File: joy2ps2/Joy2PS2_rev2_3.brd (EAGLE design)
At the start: 78.7 x 67.3 mm, 7 parts

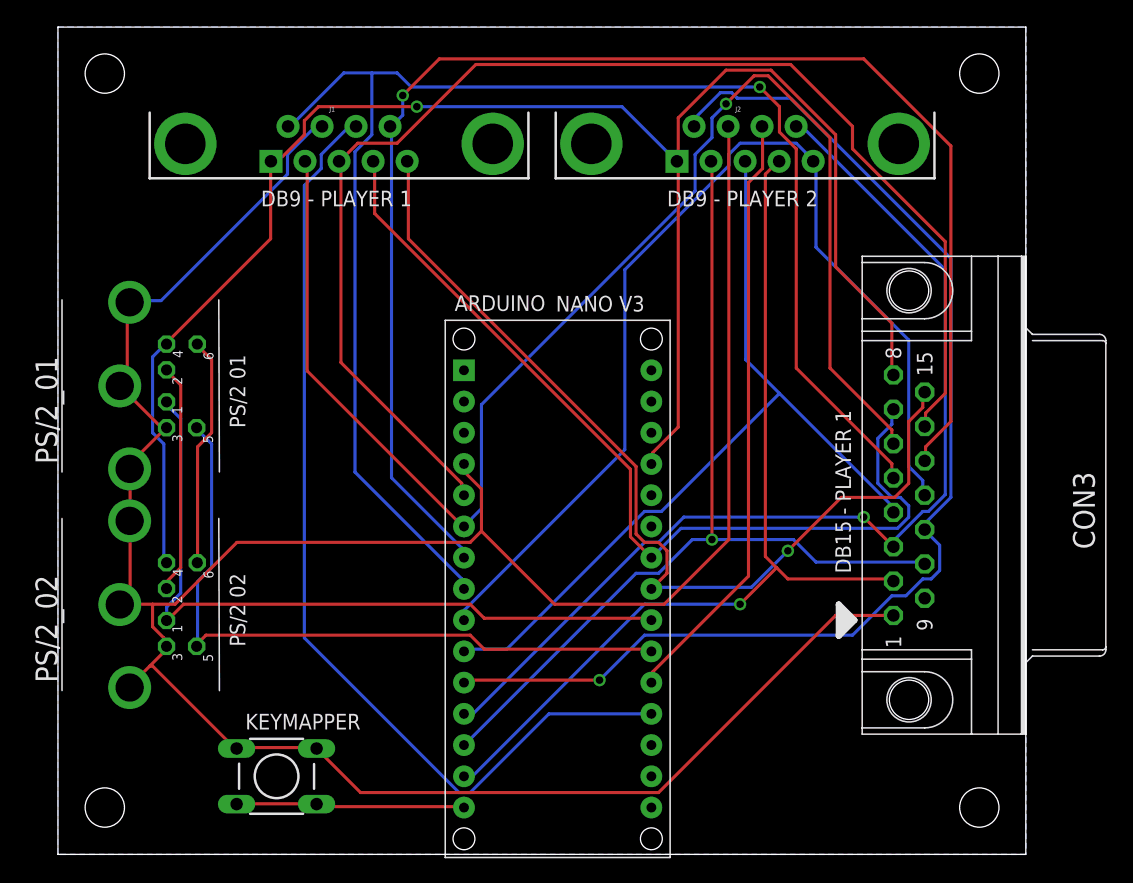
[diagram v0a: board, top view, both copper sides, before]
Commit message: Mejoras visuales
Mejora visual del esquema y corrección del fichero .BRD corrupto.
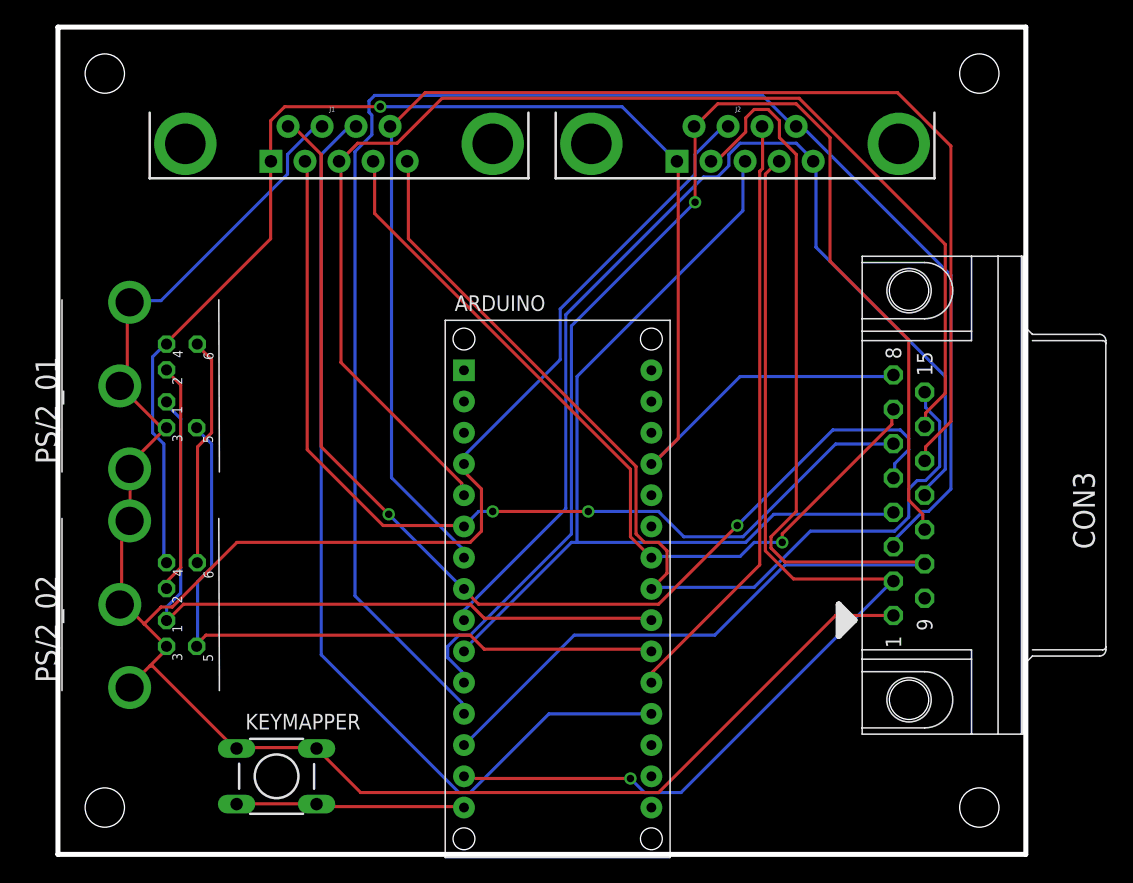
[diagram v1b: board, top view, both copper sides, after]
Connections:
- net N$1 renamed KB_DATA
- net N$10 renamed D2
- net N$11 renamed D3
- net N$12 renamed D4
- net N$13 renamed D5
- net N$14 renamed D6
- net N$15 renamed D7
- net N$16 renamed D9
- net N$17 renamed D11
- net N$18 renamed A4
- net N$19 renamed D12
- net N$2 renamed MS_DATA
- net N$20 renamed MS_CLK
- net N$3 renamed +5V
- net N$4 renamed A0
- net N$5 renamed KB_CLK
- net N$6 renamed D10
- net N$7 renamed D8
- net N$8 renamed A1
- net N$9 renamed A5
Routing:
- net D9: track 84.2 -> 132.2 mm, vias 1 -> 0
- net D3: track 116.8 -> 78.3 mm, vias 1 -> 2
- net D5: track 123.2 -> 90.5 mm, vias 1 -> 2
- net D10: track 76.0 -> 101.1 mm, vias 1 -> 0
- net GND: track 227.2 -> 205.0 mm
- net +5V: track 141.8 -> 124.1 mm
- net D11: track 76.3 -> 86.3 mm
- net D7: track 68.0 -> 76.3 mm
- net A5: track 74.7 -> 67.3 mm, vias 0 -> 1
- net D8: track 97.3 -> 102.7 mm
- net D2: track 106.7 -> 103.3 mm
- net D4: track 115.9 -> 112.6 mm, vias 1 -> 0
- net A4: track 77.2 -> 80.2 mm, vias 1 -> 0
- net D6: track 85.7 -> 87.7 mm
- net A0: track 79.8 -> 78.7 mm
- added copper zone on layer 1, net GND
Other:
- board text removed: "DB15 - PLAYER 1"
- board text removed: "DB9 - PLAYER 1"
- board text removed: "DB9 - PLAYER 2"
- board text removed: "NANO V3"
- board text removed: "PS/2 01"
- board text removed: "PS/2 02"
